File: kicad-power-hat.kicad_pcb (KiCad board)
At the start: 2 copper layers, 69.2 x 56 mm, 29 parts, among them J1 Raspberry_Pi_2_3, J2 AC Power In, J3 Screw_Terminal_01x03, Q1 BC847, Q2 BC857, Q3 BC857, U1 SP3485EEN, U2 LM2596S-5

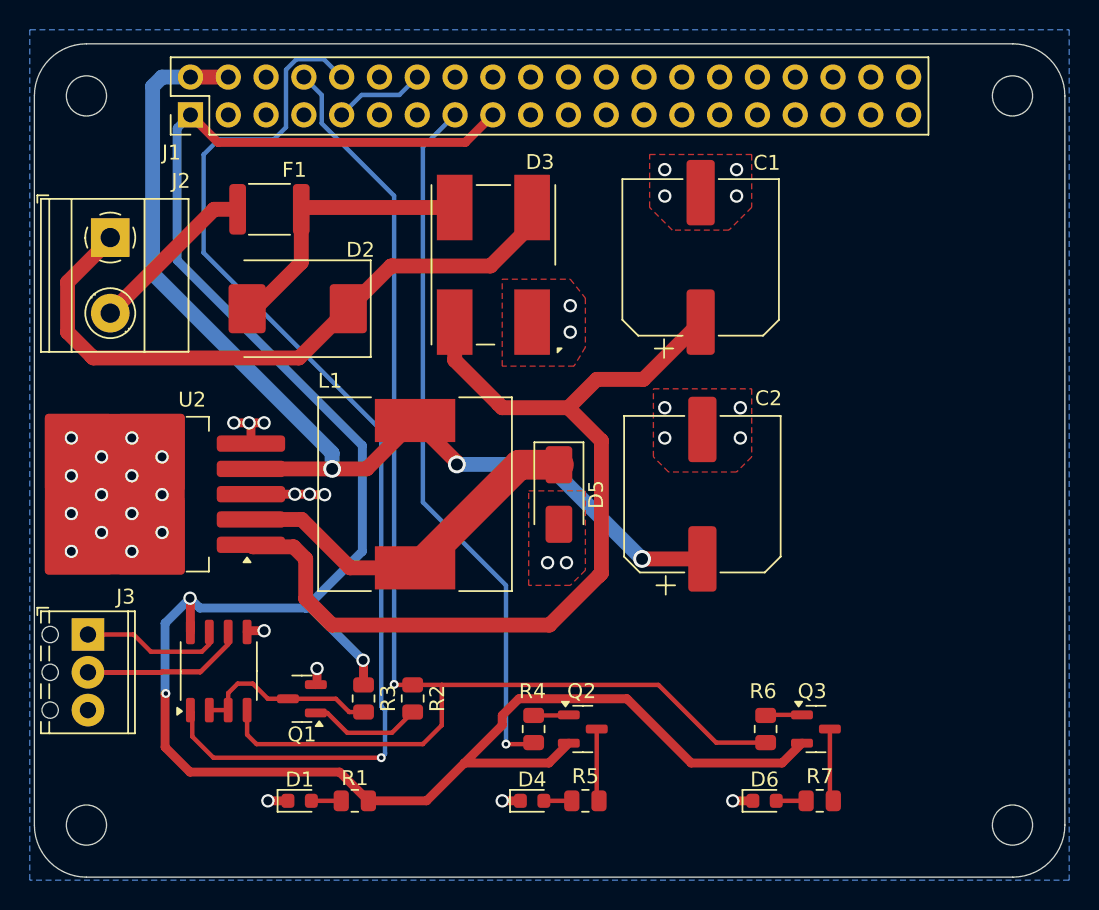
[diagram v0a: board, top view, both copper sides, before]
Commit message: wip: update to layout and labels
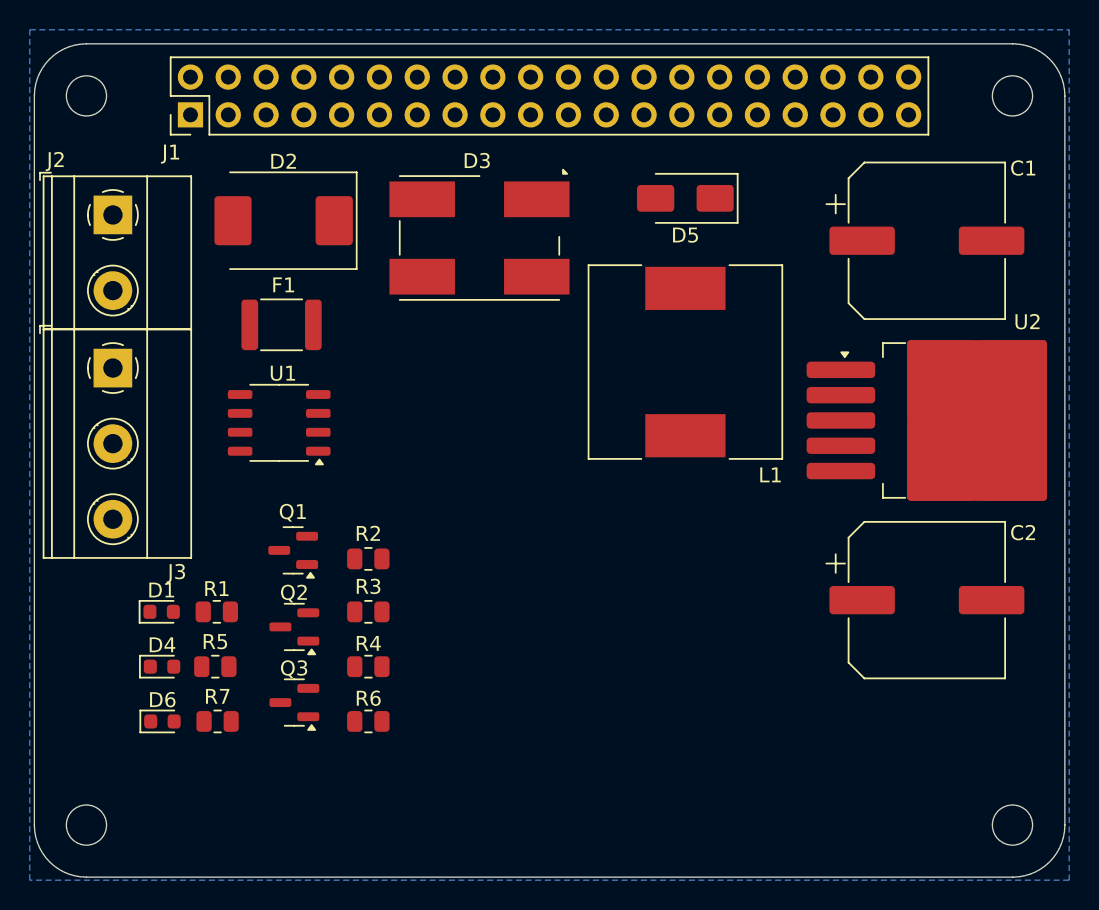
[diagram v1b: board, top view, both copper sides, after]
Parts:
- D3: value 4A -> MSB40M
- J3: footprint TerminalBlock_Phoenix:TerminalBlock_Phoenix_MPT-0,5-3-2.54_1x03_P2.54mm_Horizontal -> TerminalBlock_Phoenix:TerminalBlock_Phoenix_MKDS-1,5-3-5.08_1x03_P5.08mm_Horizontal
- moved U2 55.2 mm to (153.6, 116.4), turned to 0 degrees
- moved R7 40.8 mm to (104.1, 136.7)
- moved D6 40.8 mm to (100.4, 136.7)
- moved Q3 35.1 mm to (109.2, 135.4), turned to 180 degrees
- moved R6 26.7 mm to (114.2, 136.7), turned to 180 degrees
- moved D4 26.5 mm to (100.3, 133.0)
- moved R5 26.5 mm to (103.9, 133.0)
- moved D5 21.6 mm to (135.5, 101.5), turned to 180 degrees
- moved Q2 20.6 mm to (109.2, 130.3), turned to 180 degrees
- moved L1 20.2 mm to (135.5, 112.5), turned to -90 degrees
- moved J3 18.0 mm to (97.0, 112.9)
- moved U1 17.2 mm to (108.2, 116.6), turned to 180 degrees
- moved C2 16.7 mm to (151.7, 128.5), turned to 0 degrees
- moved R1 15.7 mm to (104.0, 129.3)
- moved D1 15.7 mm to (100.3, 129.3)
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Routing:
- net 3V3: track 147.6 -> 0.00 mm, vias 3 -> 0
- net TXD: track 88.1 -> 0.00 mm, vias 1 -> 0
- net RXD: track 75.5 -> 0.00 mm, vias 1 -> 0
- net 5V: track 71.7 -> 0.00 mm, vias 3 -> 0
- net /DC+: track 63.6 -> 0.00 mm
- net USRLED: track 47.4 -> 0.00 mm, vias 1 -> 0
- net /AC N: track 44.3 -> 0.00 mm
- net Net-(D5-K): track 24.9 -> 0.00 mm
- net GND: track 20.8 -> 0.00 mm, vias 37 -> 0
- net Net-(J3-Pin_2): track 20.2 -> 0.00 mm
- net /AC L: track 18.9 -> 0.00 mm
- net Net-(Q1-C): track 12.6 -> 0.00 mm
- net Net-(J2-Pin_2): track 11.5 -> 0.00 mm
- net Net-(J3-Pin_1): track 9.13 -> 0.00 mm
- net Net-(Q1-B): track 7.64 -> 0.00 mm
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- removed copper zone on F.Cu, net GND

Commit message: Updated pcb
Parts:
- added C3: 1u, Capacitor_SMD:C_0805_2012Metric, F.Cu at (109.3, 120.7)
- added REF**: OSHW-Symbol_6.7x6mm_SilkScreen, Symbol:OSHW-Symbol_6.7x6mm_SilkScreen, F.Cu at (102.6, 142.4)
- D2: value 30V -> SMBJ40CA
- moved D2 15.5 mm to (123.9, 104.4), turned to -90 degrees
- moved D3 13.6 mm to (135.3, 103.9)
- moved D5 9.50 mm to (135.4, 111.0)
- moved L1 8.02 mm to (135.4, 120.5)
- moved U1 3.05 mm to (111.3, 116.5)
- moved F1 2.50 mm to (106.9, 108.0)
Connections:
- J3 pad 1: Net-(J3-Pin_1) -> /RS485-A
- J3 pad 2: Net-(J3-Pin_2) -> /RS485-B
- U1 pad 6: Net-(J3-Pin_2) -> /RS485-A
- U1 pad 7: Net-(J3-Pin_1) -> /RS485-B
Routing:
- net 5V: track 0.00 -> 94.3 mm, vias 0 -> 1
- net 3V3: track 0.00 -> 83.5 mm, vias 0 -> 2
- net GND: track 0.00 -> 61.9 mm, vias 0 -> 28
- net TXD: track 0.00 -> 53.6 mm, vias 0 -> 2
- net USRLED: track 0.00 -> 40.0 mm, vias 0 -> 1
- net /AC N: track 0.00 -> 36.3 mm
- net RXD: track 0.00 -> 29.4 mm, vias 0 -> 1
- net Net-(Q1-C): track 0.00 -> 23.3 mm, vias 0 -> 2
- net /AC L: track 0.00 -> 23.0 mm
- net /DC+: track 0.00 -> 18.4 mm
- net Net-(D5-K): track 0.00 -> 15.5 mm
- net /RS485-A: track 0.00 -> 13.3 mm
- net /RS485-B: track 0.00 -> 12.0 mm
- net Net-(J2-Pin_2): track 0.00 -> 7.87 mm
- net Net-(Q1-B): track 0.00 -> 5.87 mm
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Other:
- board text added: "3V3"
- board text added: "A"
- board text added: "B"
- board text added: "GND"
- board text added: "Raspberry Power Hat + RS485 2024 - Stefano Bertelli Version 2.0"
- board text added: "TXD"
- board text added: "USR"

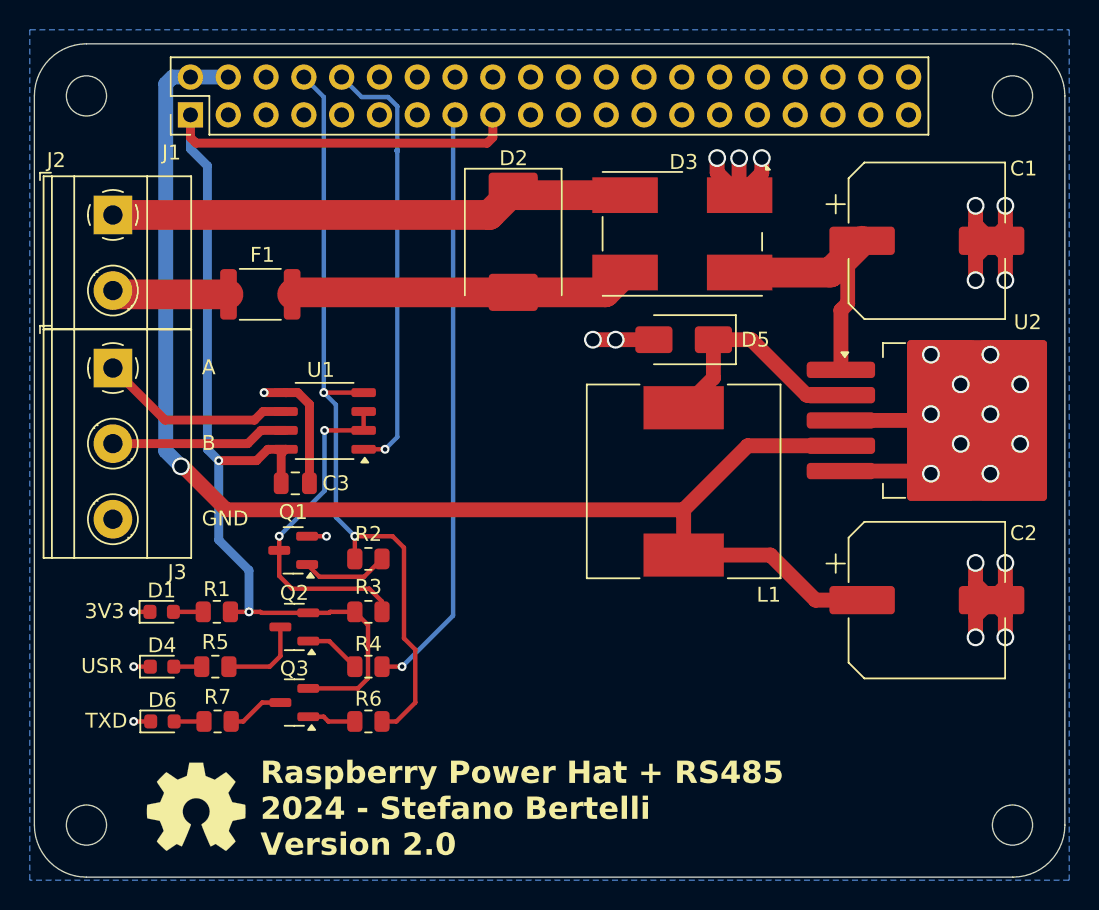
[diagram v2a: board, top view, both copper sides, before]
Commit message: fix: Update holes pattern and footprint for rectifier
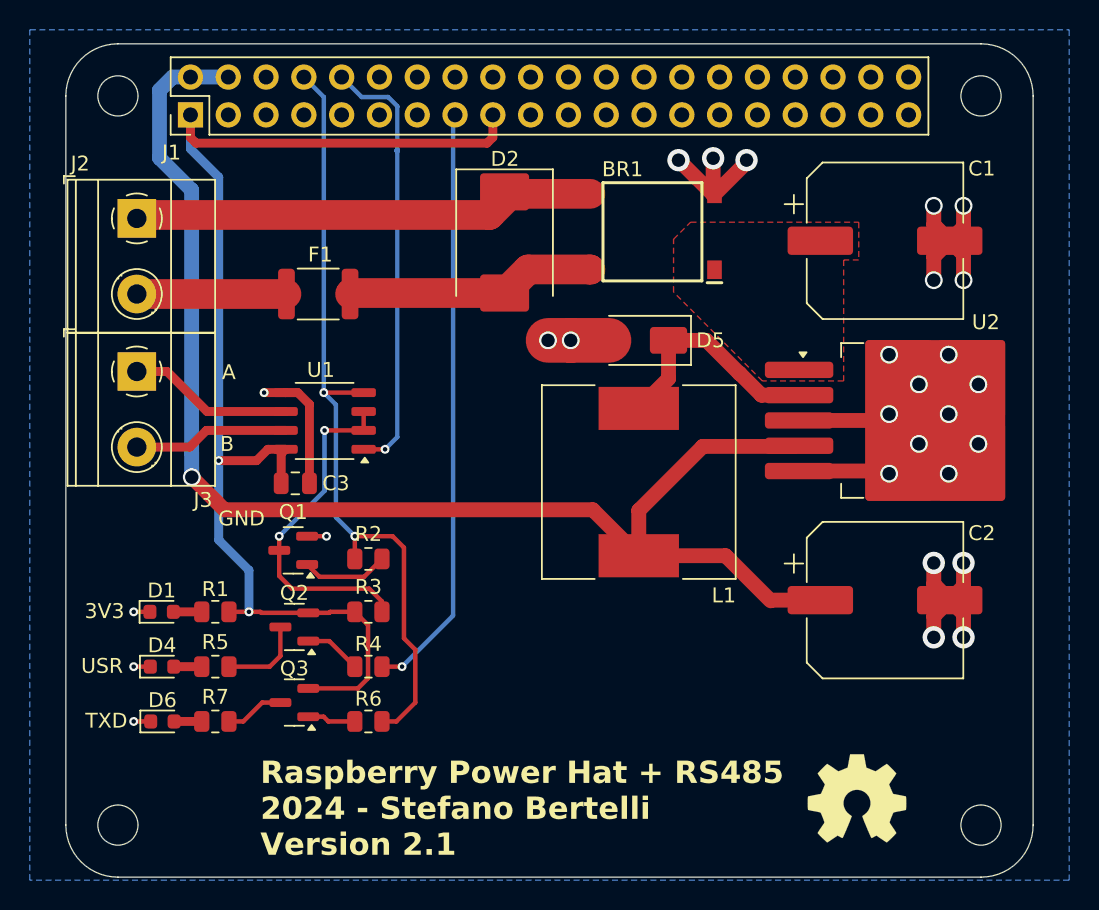
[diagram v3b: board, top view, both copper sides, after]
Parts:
- removed D3: MSB40M, Diode_SMD:Diode_Bridge_Bourns_CD-DF4xxS
- added BR1: MSB40M, SamacSys_Parts:SOTFL510P865X150-4N, F.Cu at (133.3, 103.7)
- D2: value SMBJ40CA -> SMDJ40CA
- J3: value Screw_Terminal_01x03 -> RS485; footprint TerminalBlock_Phoenix:TerminalBlock_Phoenix_MKDS-1,5-3-5.08_1x03_P5.08mm_Horizontal -> TerminalBlock_Phoenix:TerminalBlock_Phoenix_MKDS-1,5-2-5.08_1x02_P5.08mm_Horizontal
- moved REF** 44.4 mm to (147.0, 141.8)
- moved F1 3.89 mm to (110.8, 107.9)
- moved D5 3.02 mm to (132.4, 111.0)
- moved L1 3.02 mm to (132.4, 120.6)
- moved C1 2.81 mm to (148.9, 104.3)
- moved C2 2.81 mm to (148.9, 128.5)
- moved U2 2.81 mm to (150.8, 116.4)
- moved H1 2.11 mm to (97.4, 94.6)
- moved H3 2.11 mm to (97.4, 143.6)
- moved H2 2.11 mm to (155.4, 94.6)
- moved H4 2.11 mm to (155.4, 143.6)
- moved J2 1.62 mm to (98.6, 102.8)
- moved J3 1.62 mm to (98.6, 113.1)
- moved D2 0.58 mm to (123.3, 104.5)
- moved R7 0.15 mm to (103.9, 136.7)
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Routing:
- net /DC+: track 18.4 -> 0.00 mm
- net /AC L: track 23.0 -> 16.8 mm
- net /AC N: track 36.3 -> 31.9 mm
- net Net-(J2-Pin_2): track 7.87 -> 10.4 mm
- net /RS485-A: track 13.3 -> 11.1 mm
- net 5V: track 94.3 -> 92.7 mm
- net /RS485-B: track 12.0 -> 10.8 mm
- net Net-(D6-A): track 2.01 -> 2.67 mm
- net Net-(D5-K): track 15.5 -> 15.0 mm
- added copper zone on F.Cu, net /DC+
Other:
- board size 69.2 x 56 mm -> 65 x 56 mm
- board text added: "Raspberry Power Hat + RS485 2024 - Stefano Bertelli Version 2.1"
- board text removed: "Raspberry Power Hat + RS485 2024 - Stefano Bertelli Version 2.0"
